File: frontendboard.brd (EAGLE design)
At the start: 158.7 x 58.1 mm, 64 parts, among them U1 MAX2769, X3 BU-SMA-H

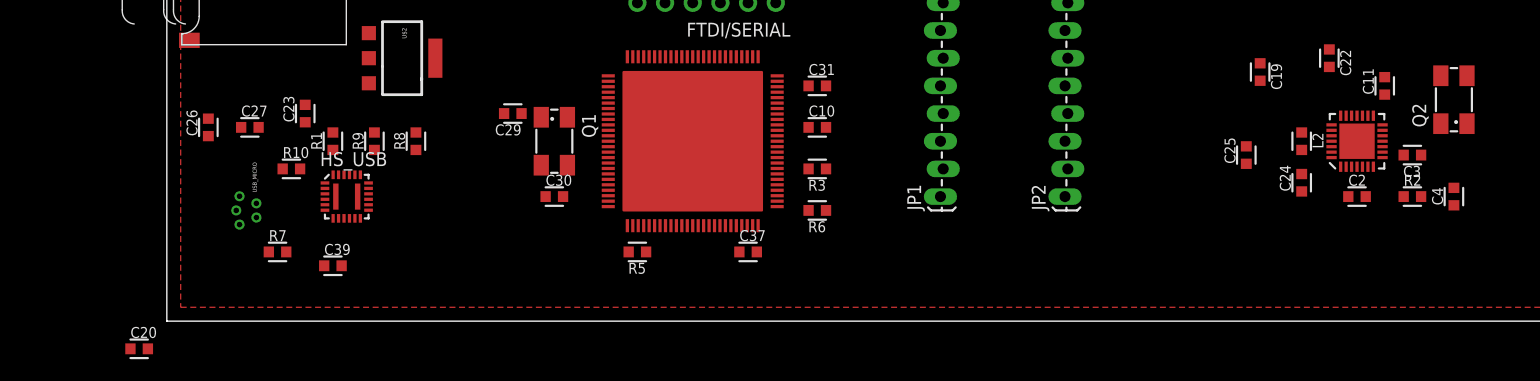
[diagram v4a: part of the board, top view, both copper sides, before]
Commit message: All ERC errors and warnings fixed or approved. No LEDs in place.
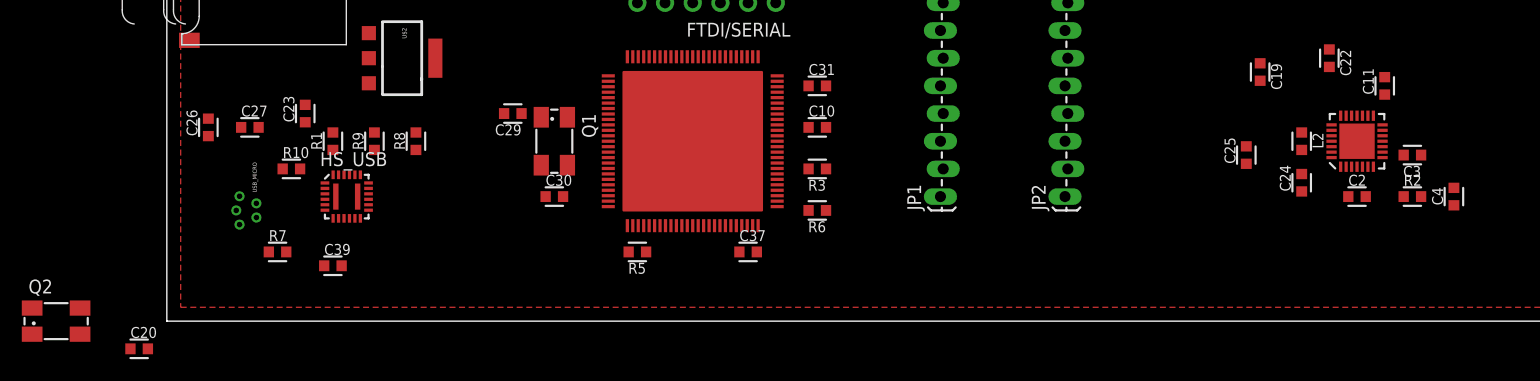
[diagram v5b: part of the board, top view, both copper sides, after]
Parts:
- C10, C11: value (none) -> 10nF
- moved Q2 129.9 mm to (-10.2, 0.00), turned to 0 degrees
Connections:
- net BAR_GND: now also Q2.3; no longer Q2.1
- net N$3: now also Q2.1; no longer Q2.3
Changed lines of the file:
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@@
 <element name="C7" library="rcl_custom" package="0603-B" value="0.1uF" x="21.59" y="49.53"/>
 <element name="C9" library="rcl_custom" package="0603-B" value="0.1uF" x="33.02" y="53.34"/>
-<element name="C10" library="rcl_custom" package="0603-B" value="" x="59.69" y="17.78"/>
-<element name="C11" library="rcl_custom" package="0603-B" value="" x="111.76" y="21.59" rot="R90"/>
+<element name="C10" library="rcl_custom" package="0603-B" value="10nF" x="59.69" y="17.78"/>
+<element name="C11" library="rcl_custom" package="0603-B" value="10nF" x="111.76" y="21.59" rot="R90"/>
 <element name="C15" library="rcl_custom" package="0603-B" value="0.1uF" x="3.81" y="48.26"/>
 <element name="C16" library="rcl_custom" package="0603-B" value="0.1nF" x="3.81" y="43.18"/>
@@
 <element name="C38" library="rcl_custom" package="0603-B" value="100nF" x="34.29" y="40.64" rot="R180"/>
 <element name="C39" library="rcl_custom" package="0603-B" value="1uF" x="15.24" y="5.08"/>
-<element name="Q2" library="crystal" package="CTS406" value="" x="118.11" y="20.32" rot="R90">
-<attribute name="OC_NEWARK" value="unknown" x="163.83" y="81.28" size="1.778" layer="27" rot="R90" display="off"/>
-<attribute name="MPN" value="" x="163.83" y="81.28" size="1.778" layer="27" rot="R90" display="off"/>
-<attribute name="MF" value="" x="163.83" y="81.28" size="1.778" layer="27" rot="R90" display="off"/>
-<attribute name="OC_FARNELL" value="unknown" x="163.83" y="81.28" size="1.778" layer="27" rot="R90" display="off"/>
+<element name="C20" library="rcl_custom" package="0603-B" value="2.2uF" x="-2.54" y="-2.54"/>
+<element name="Q2" library="crystal" package="CTS406" value="" x="-10.16" y="0">
+<attribute name="OC_NEWARK" value="unknown" x="-10.16" y="0" size="1.778" layer="27" display="off"/>
+<attribute name="MPN" value="" x="-10.16" y="0" size="1.778" layer="27" display="off"/>
+<attribute name="MF" value="" x="-10.16" y="0" size="1.778" layer="27" display="off"/>
+<attribute name="OC_FARNELL" value="unknown" x="-10.16" y="0" size="1.778" layer="27" display="off"/>
 </element>
-<element name="C20" library="rcl_custom" package="0603-B" value="2.2uF" x="-2.54" y="-2.54"/>
 </elements>
 <signals>
@@
 <vertex x="157.48" y="1.27"/>
 </polygon>
-<contactref element="Q2" pad="1"/>
 <contactref element="C20" pad="1"/>
 <contactref element="U$5" pad="CD2"/>
 <contactref element="U1" pad="BODY"/>
+<contactref element="Q2" pad="3"/>
 <wire x1="115.5799" y1="34.2801" x2="115.5799" y2="39.3799" width="0" layer="19" extent="1-1"/>
 <wire x1="110.4801" y1="39.3799" x2="115.5799" y2="39.3799" width="0" layer="19" extent="1-1"/>
 <wire x1="110.4801" y1="34.2801" x2="115.5799" y2="34.2801" width="0" layer="19" extent="1-1"/>
-<wire x1="119.31" y1="18.12" x2="115.5799" y2="34.2801" width="0" layer="19" extent="1-1"/>
-<wire x1="118.11" y1="12.23" x2="119.31" y2="18.12" width="0" layer="19" extent="1-1"/>
-<wire x1="113.5" y1="15.24" x2="118.11" y2="12.23" width="0" layer="19" extent="1-1"/>
-<wire x1="109.22" y1="16.51" x2="113.5" y2="15.24" width="0" layer="19" extent="1-1"/>
+<wire x1="94.22" y1="42.67" x2="110.4801" y2="39.3799" width="0" layer="19" extent="1-1"/>
+<wire x1="109.22" y1="16.51" x2="110.4801" y2="34.2801" width="0" layer="19" extent="1-1"/>
+<wire x1="113.5" y1="15.24" x2="109.22" y2="16.51" width="0" layer="19" extent="1-1"/>
+<wire x1="118.11" y1="12.23" x2="113.5" y2="15.24" width="0" layer="19" extent="1-1"/>
 <wire x1="104.14" y1="13.5" x2="109.22" y2="16.51" width="0" layer="19" extent="1-1"/>
 <wire x1="99.06" y1="16.04" x2="104.14" y2="13.5" width="0" layer="19" extent="1-1"/>
-<wire x1="94.22" y1="42.67" x2="110.4801" y2="39.3799" width="0" layer="19" extent="1-1"/>
 <wire x1="60.49" y1="17.78" x2="99.06" y2="16.04" width="0" layer="19" extent="1-1"/>
 <wire x1="60.49" y1="13.97" x2="60.49" y2="17.78" width="0" layer="19" extent="1-1"/>
@@
 <wire x1="54.61" y1="49.53" x2="49.53" y2="49.53" width="0" layer="19" extent="1-1"/>
 <wire x1="-3.34" y1="-2.54" x2="6.67" y2="8.86" width="0" layer="19" extent="1-1"/>
+<wire x1="-7.96" y1="1.2" x2="-3.34" y2="-2.54" width="0" layer="19" extent="1-1"/>
 </signal>
 <signal name="N$2">
@@
 <signal name="N$3">
 <contactref element="C11" pad="2"/>
-<contactref element="Q2" pad="3"/>
-<wire x1="111.76" y1="22.39" x2="116.91" y2="22.52" width="0" layer="19" extent="1-1"/>
+<contactref element="Q2" pad="1"/>
+<wire x1="-12.36" y1="-1.2" x2="111.76" y2="22.39" width="0" layer="19" extent="1-1"/>
 </signal>
 <signal name="USB_D-">

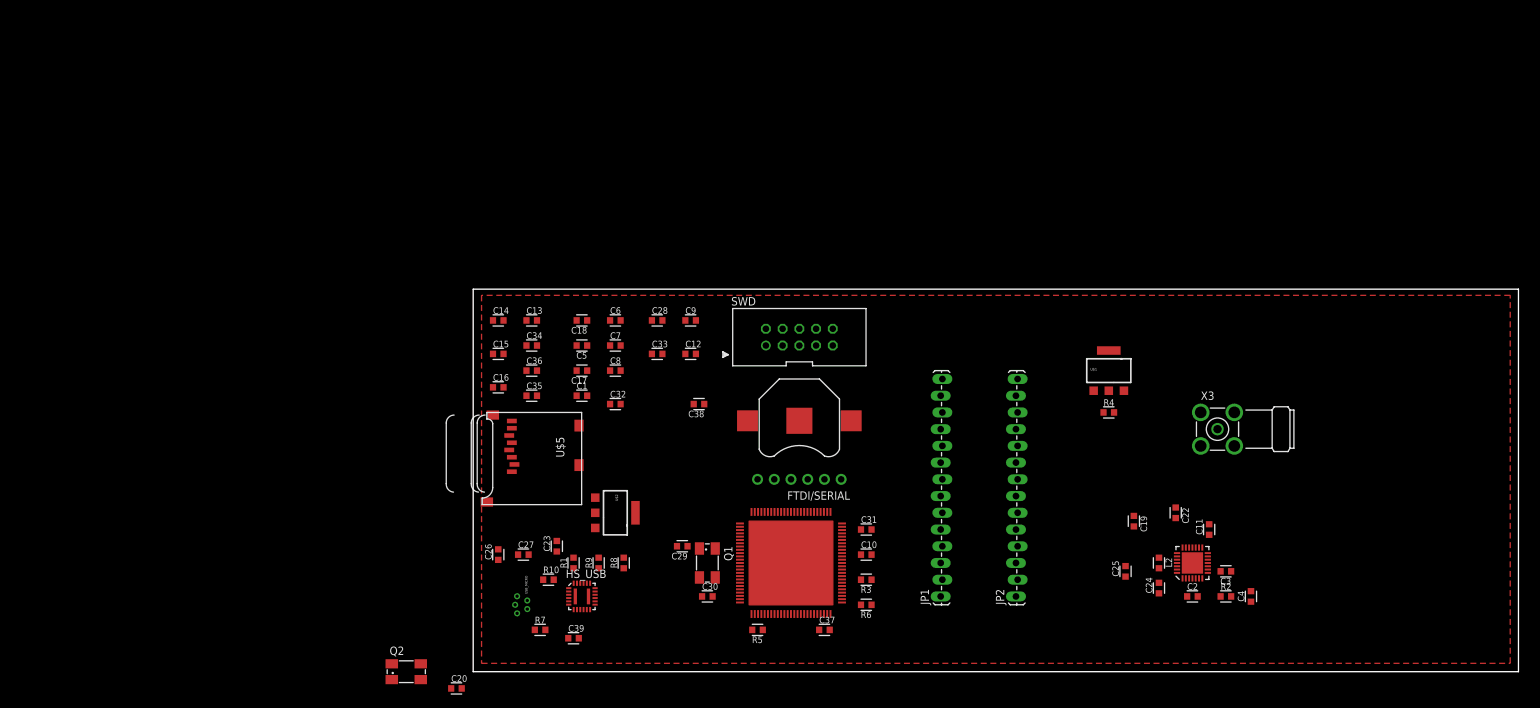
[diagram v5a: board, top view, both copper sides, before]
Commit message: Start layout on RF side.
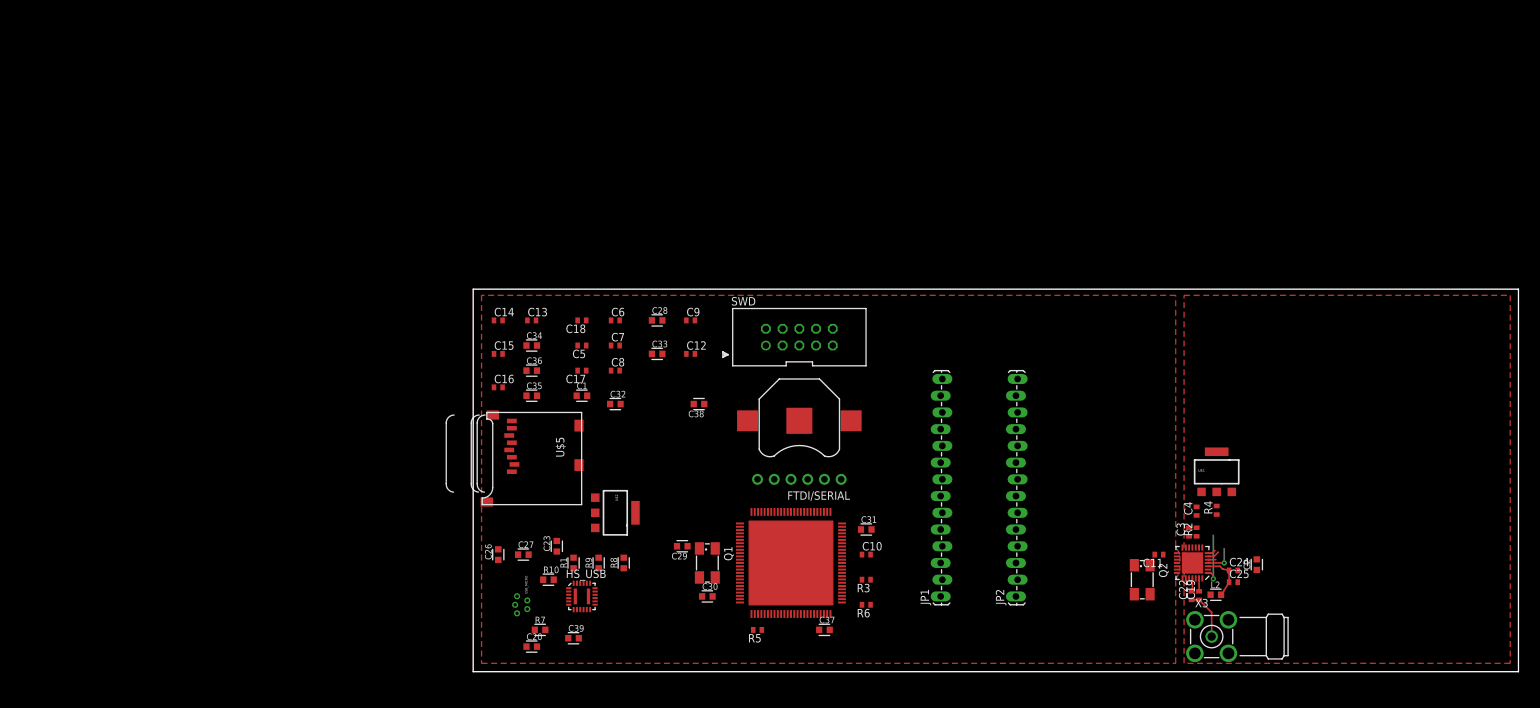
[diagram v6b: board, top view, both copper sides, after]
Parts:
- C10, C11, C12, C13, C14, C15, C16, C17, C18, C19, C22, C24, C25, C3, C4, C5, C6, C7, C8, C9: device rcl_custom:0603-B -> rcl:C0402
- R2, R3, R4, R5, R6: device rcl_custom:0603-B -> rcl:R0402
- moved Q2 112.6 mm to (101.6, 14.0), turned to 270 degrees
- moved X3 31.5 mm to (112.1, 5.33)
- moved U$1 22.5 mm to (112.9, 30.4)
- moved R4 22.1 mm to (112.9, 24.5), turned to 90 degrees
- moved C25 16.5 mm to (115.4, 13.6), turned to 0 degrees
- moved C4 15.4 mm to (109.9, 24.4)
- moved C19 15.0 mm to (110.2, 11.6), turned to 90 degrees
- moved C20 13.1 mm to (8.89, 3.81)
- moved C22 12.8 mm to (109.1, 11.6), turned to 90 degrees
- moved C24 11.6 mm to (115.4, 15.4), turned to 0 degrees
- moved C2 10.9 mm to (119.0, 16.3), turned to 90 degrees
- moved R2 10.7 mm to (109.9, 21.2), turned to 90 degrees
- moved L2 9.89 mm to (112.8, 11.7), turned to 0 degrees
- moved C11 8.52 mm to (104.1, 17.8), turned to 180 degrees
- moved C3 8.18 mm to (108.7, 21.2), turned to 90 degrees
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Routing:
- net ANTFLAG: track 0.00 -> 8.11 mm, vias 0 -> 1
- net N$1: track 0.00 -> 7.51 mm
- net ANTBIAS: track 0.00 -> 7.48 mm
- net 3.3VA: track 0.00 -> 4.65 mm, vias 0 -> 1
- net LNA2: track 0.00 -> 2.02 mm
- net LNA1: track 0.00 -> 1.97 mm
- net LD: track 0.00 -> 1.87 mm
- net SHDN: track 0.00 -> 1.26 mm
- net N$2: track 0.00 -> 1.21 mm
